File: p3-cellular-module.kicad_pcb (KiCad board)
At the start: 4 copper layers, 40 x 57.4 mm, 57 parts, among them J1 Conn_Coaxial, J2 SIM8060-6-1-14-00-A, J4 Pogo Pins, Q1 BC818, SW1 KMR221GLFS, U1 AP62301WU7, U2 EG25G, U3 USBLC6-2SC6

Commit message: Add: Improved layout
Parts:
- removed J1: Conn_Coaxial, Connector_Coaxial:U.FL_Hirose_U.FL-R-SMT-1_Vertical
- removed R13, R14: DNF, Resistor_SMD:R_0402_1005Metric
- removed TP3: DCD, TestPoint:TestPoint_Pad_D1.5mm
- removed TP4: CTS, TestPoint:TestPoint_Pad_D1.5mm
- removed TP5: RTS, TestPoint:TestPoint_Pad_D1.5mm
- removed TP6: DTR, TestPoint:TestPoint_Pad_D1.5mm
- added E1: NN02-201, NN02-201:XCVR_NN02-201, B.Cu at (130.1, 106.3)
- added REF**: MountingHole_2.2mm_M2_DIN965_Pad, MountingHole:MountingHole_2.2mm_M2_DIN965_Pad, F.Cu at (145.1, 90.9)
- Q1, R5, R6, R7: moved to F.Cu
- TP1, TP10, TP7, TP8, TP9: footprint TestPoint:TestPoint_Pad_D1.5mm -> TestPoint:TestPoint_Pad_1.0x1.0mm
- TP2: value RI -> 3V8; footprint TestPoint:TestPoint_Pad_D1.5mm -> TestPoint:TestPoint_Pad_1.0x1.0mm
- moved TP2 27.2 mm to (133.7, 114.7), turned to 0 degrees
- moved D1 7.38 mm to (135.6, 92.5), turned to 180 degrees
- moved U3 7.37 mm to (140.2, 91.2), turned to -90 degrees
- moved Q1 7.12 mm to (132.0, 90.3), turned to 90 degrees
- moved R7 7.08 mm to (135.5, 90.8)
- moved C18 6.76 mm to (158.8, 109.6), turned to 0 degrees
- moved D2 5.78 mm to (161.8, 106.4)
- moved TP7 5.15 mm to (133.2, 127.0), turned to 90 degrees
- moved R5 3.65 mm to (131.8, 93.2), turned to 0 degrees
- moved R6 3.48 mm to (135.5, 89.1)
- moved R10 3.21 mm to (154.8, 112.1), turned to -90 degrees
- moved TP8 3.01 mm to (133.2, 129.2), turned to 90 degrees
- moved R4 3.00 mm to (161.1, 112.0)
- moved L2 2.30 mm to (128.7, 111.4), turned to -90 degrees
- moved C14 2.06 mm to (131.1, 110.5), turned to 0 degrees
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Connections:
- TP2 pad 1: Net-(TP2-Pad1) -> +3V8
- U2 pad 62: Net-(TP2-Pad1) -> unconnected-(U2-Pad62)
- U2 pad 63: Net-(TP3-Pad1) -> unconnected-(U2-Pad63)
- U2 pad 64: Net-(TP4-Pad1) -> unconnected-(U2-Pad64)
- U2 pad 65: Net-(TP5-Pad1) -> unconnected-(U2-Pad65)
- U2 pad 66: Net-(TP6-Pad1) -> unconnected-(U2-Pad66)
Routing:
- net /Cellular Modem/USIM_RST: track 0.00 -> 43.7 mm, vias 0 -> 1
- net /Cellular Modem/USIM_VDD: track 7.53 -> 46.9 mm, vias 0 -> 7
- net /Cellular Modem/USIM_CLK: track 0.00 -> 32.6 mm, vias 0 -> 1
- net /Cellular Modem/USIM_DATA: track 0.00 -> 29.5 mm, vias 0 -> 1
- net Net-(TP8-Pad1): track 0.00 -> 28.1 mm, vias 0 -> 3
- net Net-(TP7-Pad1): track 0.00 -> 27.8 mm, vias 0 -> 3
- net Net-(C17-Pad1): track 0.00 -> 17.3 mm
- net VBUS: track 15.0 -> 31.5 mm, vias 17 -> 15
- net Net-(C18-Pad1): track 0.45 -> 12.8 mm, vias 0 -> 2
- net +3V8: track 0.00 -> 12.2 mm, vias 10 -> 12
- net Net-(C15-Pad1): track 0.00 -> 11.2 mm, vias 0 -> 2
- net Net-(R2-Pad2): track 0.00 -> 10.1 mm, vias 0 -> 2
- net /USB Connector/USB_DN_RAW: track 6.91 -> 16.0 mm
- net /USB Connector/USB_DP_RAW: track 4.87 -> 12.5 mm
- net Net-(D2-Pad1): track 0.00 -> 7.42 mm, vias 0 -> 2
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- added copper zone on In1.Cu, net VBUS
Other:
- board size 40 x 57.4 mm -> 42 x 57.5 mm
- board text added: "5V"
- board text added: "G"
- board text added: "GND"
- board text added: "LED"
- board text added: "PKY"
- board text added: "U+"
- board text added: "U-"

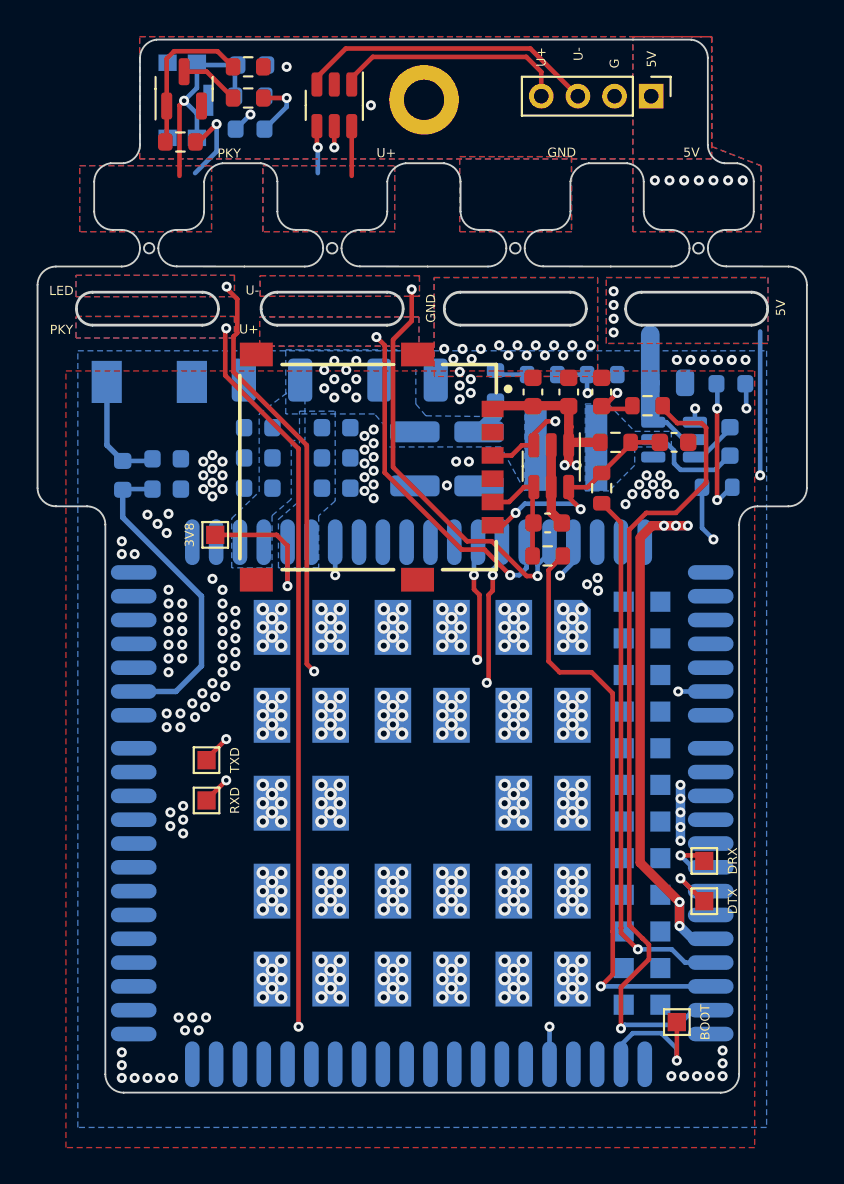
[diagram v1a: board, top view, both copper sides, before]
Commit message: Update: Ground plane setup
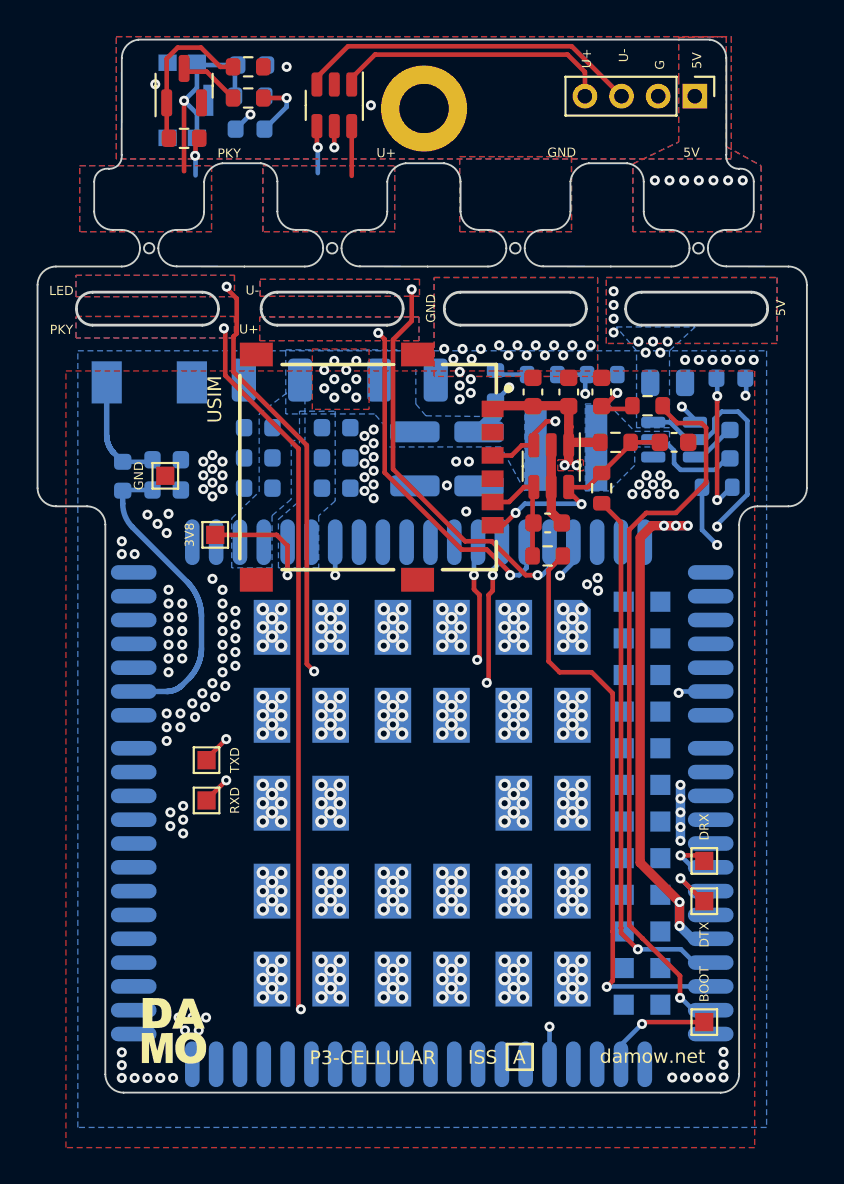
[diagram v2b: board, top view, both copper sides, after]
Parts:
- added G***: LOGO, LOGO, F.Cu at (131.4, 141.7)
- added TP3: GND, TestPoint:TestPoint_Pad_1.0x1.0mm, F.Cu at (131.0, 111.4)
- REF**: value MountingHole_2.2mm_M2_DIN965_Pad -> MountingHole_2.7mm_M2.5_DIN965_Pad; footprint MountingHole:MountingHole_2.2mm_M2_DIN965_Pad -> MountingHole:MountingHole_2.7mm_M2.5_DIN965_Pad
- moved J4 2.38 mm to (159.9, 90.7)
- moved TP1 1.50 mm to (160.4, 141.2)
- moved REF** 0.47 mm to (145.1, 91.4)
- moved D2 0.30 mm to (161.8, 106.1)
- moved R5 0.28 mm to (132.0, 93.0)
- moved Q1 0.17 mm to (132.0, 90.1)
- moved C2 0.15 mm to (161.8, 109.7)
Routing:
- net +3V8: track 12.2 -> 25.6 mm, vias 12 -> 13
- net VBUS: track 31.5 -> 26.2 mm, vias 15 -> 20
- net /Cellular Modem/USIM_RST: track 43.7 -> 38.8 mm
- net /Cellular Modem/NET_STAT_DRV: track 50.0 -> 47.1 mm
- net /USB Connector/USB_DN_RAW: track 16.0 -> 18.5 mm
- net /USB Connector/USB_DP_RAW: track 12.5 -> 15.0 mm
- net Net-(TP7-Pad1): track 27.8 -> 26.2 mm
- net Net-(TP1-Pad1): track 6.42 -> 5.07 mm
- net /Cellular Modem/PWRKEY: track 68.1 -> 67.1 mm
- net /Cellular Modem/USIM_VDD: track 46.9 -> 46.0 mm
- net GND: vias 362 -> 364
- added copper zone on F.Cu, net +3V8
- added copper zone on F.Cu, net /Cellular Modem/USIM_VDD
- added copper zone on In1.Cu, net /Cellular Modem/USIM_VDD
- added copper zone on In1.Cu, net GND
- removed copper zone on In1.Cu, net +3V8
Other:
- outline, holes or cut-outs redrawn
- board text added: "A"
- board text added: "ISS"
- board text added: "P3-CELLULAR"
- board text added: "USIM"
- board text added: "damow.net"

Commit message: Add: Board size changes
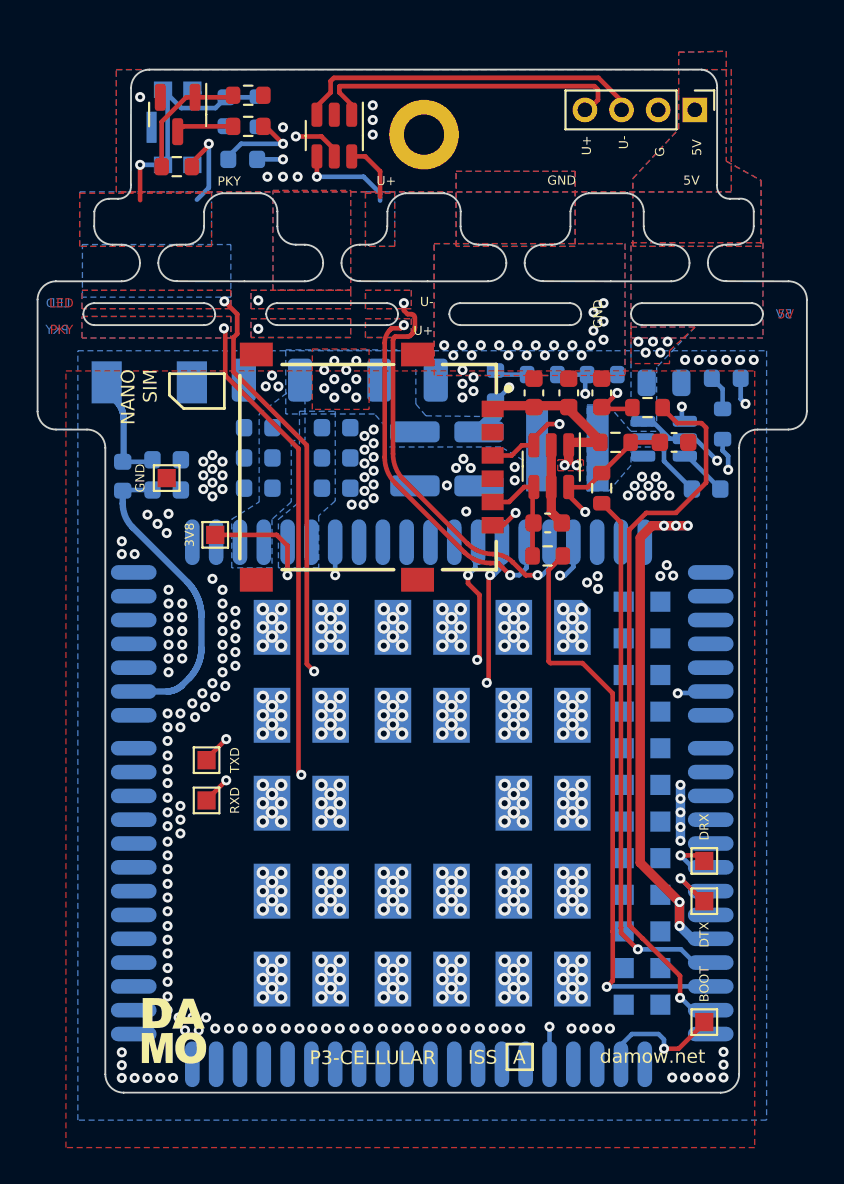
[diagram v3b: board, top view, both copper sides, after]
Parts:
- REF**: value MountingHole_2.7mm_M2.5_DIN965_Pad -> MountingHole_2.2mm_M2_DIN965_Pad; footprint MountingHole:MountingHole_2.7mm_M2.5_DIN965_Pad -> MountingHole:MountingHole_2.2mm_M2_DIN965_Pad
- moved R4 3.46 mm to (161.4, 108.6), turned to -90 degrees
- moved D3 2.91 mm to (134.3, 91.5), turned to 90 degrees
- moved C2 2.77 mm to (160.5, 112.2), turned to 180 degrees
- moved C4 1.96 mm to (153.0, 106.9)
- moved C13 1.90 mm to (151.1, 106.9)
- moved D1 1.70 mm to (135.2, 94.2), turned to 0 degrees
- moved U3 1.65 mm to (140.2, 92.8)
- moved Q1 1.61 mm to (131.7, 91.7), turned to -90 degrees
- moved R5 1.60 mm to (131.6, 94.5)
- moved R6 1.55 mm to (135.5, 90.7)
- moved R7 1.55 mm to (135.5, 92.3)
- moved SW1 1.50 mm to (131.7, 92.4), turned to -90 degrees
- moved REF** 1.42 mm to (145.1, 92.8)
- moved R15 0.96 mm to (136.1, 91.5), turned to -90 degrees
- moved J4 0.75 mm to (159.9, 91.5)
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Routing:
- net Net-(D2-Pad1): track 7.44 -> 1.92 mm, vias 2 -> 0
- net VBUS: track 26.2 -> 22.8 mm, vias 20 -> 9
- net /Cellular Modem/USB_DN: track 24.7 -> 27.4 mm
- net /USB Connector/USB_DP_RAW: track 15.0 -> 17.5 mm
- net /Cellular Modem/NET_STAT_DRV: track 47.1 -> 49.4 mm
- net /Cellular Modem/STAT_OD: track 27.4 -> 29.5 mm
- net /Power Supply/SW: track 5.58 -> 3.58 mm
- net Net-(Q1-Pad1): track 8.78 -> 6.95 mm
- net Net-(D1-Pad1): track 3.48 -> 4.96 mm
- net /Cellular Modem/USB_DP: track 21.7 -> 22.9 mm
- net /Cellular Modem/PWRKEY: track 67.1 -> 68.2 mm
- net Net-(C14-Pad1): track 6.15 -> 5.15 mm
- net Net-(TP1-Pad1): track 5.07 -> 6.05 mm
- net /USB Connector/USB_DN_RAW: track 18.5 -> 19.1 mm
- net /Cellular Modem/USIM_VDD: track 46.0 -> 46.5 mm
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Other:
- board size 42 x 57.5 mm -> 42 x 55.8 mm
- board text added: "NANO SIM"
- board text removed: "USIM"

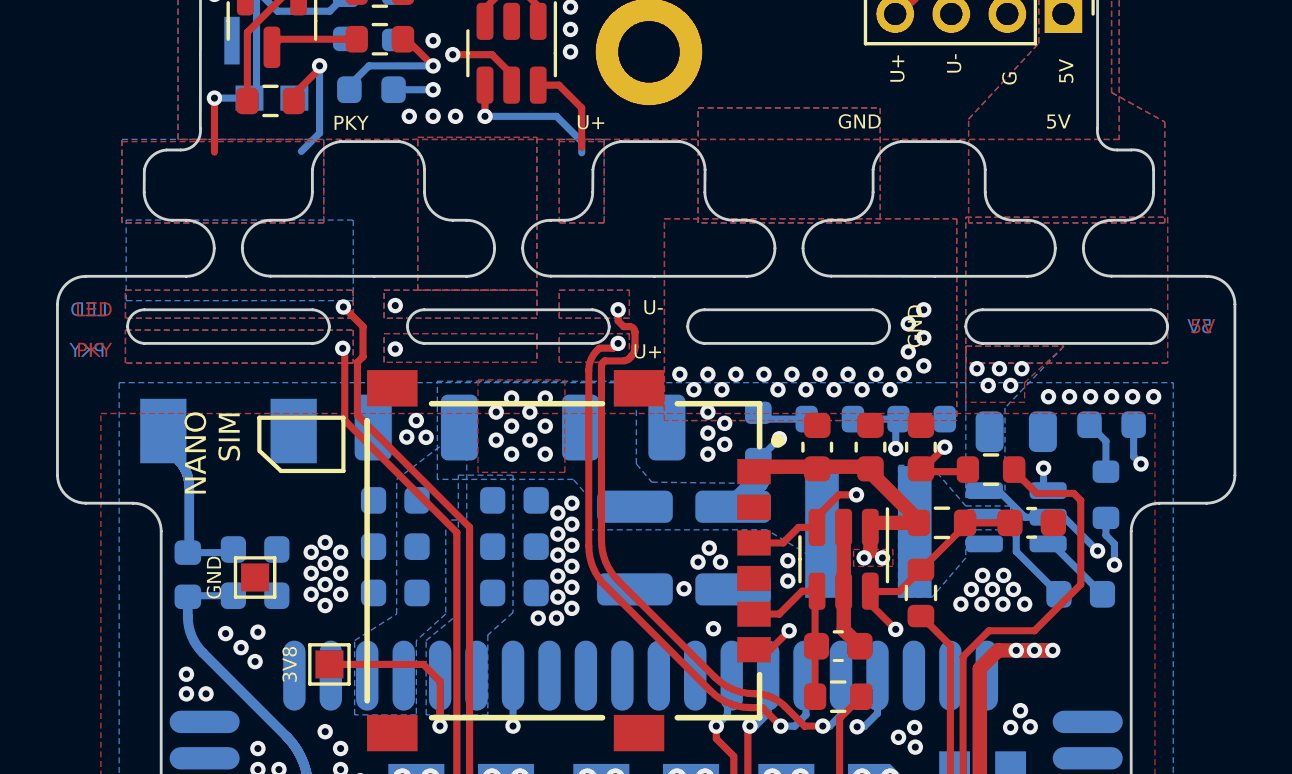
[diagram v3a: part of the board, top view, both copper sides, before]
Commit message: Add: Mechanical changes pre-rev1 production run
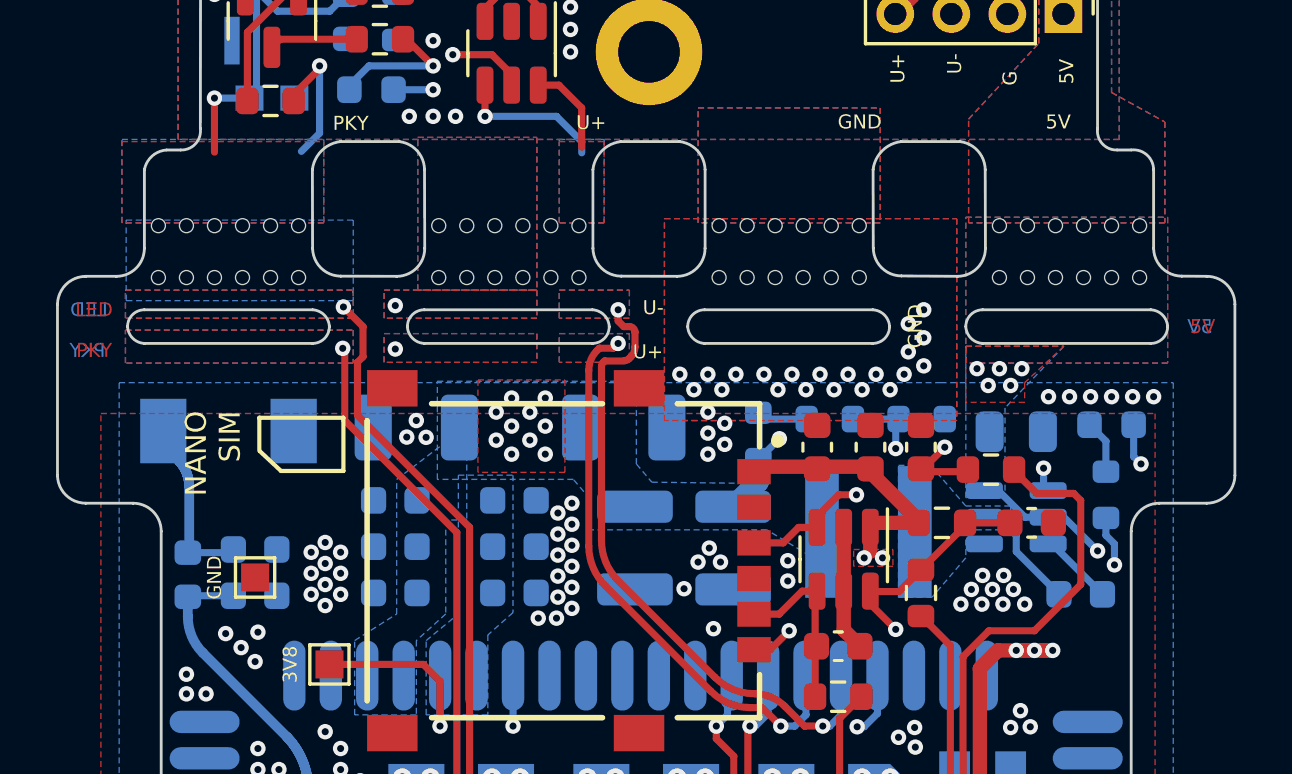
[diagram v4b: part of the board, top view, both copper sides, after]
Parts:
- added REF**: MouseBitHole_0.5mm, p3-cellular-module:MouseBitHole_0.5mm, F.Cu at (141.6, 99.0)
- added REF**: MouseBitHole_0.5mm, p3-cellular-module:MouseBitHole_0.5mm, F.Cu at (147.6, 99.0)
- added REF**: MouseBitHole_0.5mm, p3-cellular-module:MouseBitHole_0.5mm, F.Cu at (128.6, 100.8)
- added REF**: MouseBitHole_0.5mm, p3-cellular-module:MouseBitHole_0.5mm, F.Cu at (132.6, 100.8)
- added REF**: MouseBitHole_0.5mm, p3-cellular-module:MouseBitHole_0.5mm, F.Cu at (159.6, 100.8)
- added REF**: MouseBitHole_0.5mm, p3-cellular-module:MouseBitHole_0.5mm, F.Cu at (127.6, 99.0)
- added REF**: MouseBitHole_0.5mm, p3-cellular-module:MouseBitHole_0.5mm, F.Cu at (132.6, 99.0)
- added REF**: MouseBitHole_0.5mm, p3-cellular-module:MouseBitHole_0.5mm, F.Cu at (141.6, 100.8)
- added REF**: MouseBitHole_0.5mm, p3-cellular-module:MouseBitHole_0.5mm, F.Cu at (162.6, 99.0)
- added REF**: MouseBitHole_0.5mm, p3-cellular-module:MouseBitHole_0.5mm, F.Cu at (142.6, 100.8)
- added REF**: MouseBitHole_0.5mm, p3-cellular-module:MouseBitHole_0.5mm, F.Cu at (149.6, 99.0)
- added REF**: MouseBitHole_0.5mm, p3-cellular-module:MouseBitHole_0.5mm, F.Cu at (148.6, 100.8)
- added REF**: MouseBitHole_0.5mm, p3-cellular-module:MouseBitHole_0.5mm, F.Cu at (139.6, 100.8)
- added REF**: MouseBitHole_0.5mm, p3-cellular-module:MouseBitHole_0.5mm, F.Cu at (152.6, 100.8)
- added REF**: MouseBitHole_0.5mm, p3-cellular-module:MouseBitHole_0.5mm, F.Cu at (131.6, 100.8)
- added REF**: MouseBitHole_0.5mm, p3-cellular-module:MouseBitHole_0.5mm, F.Cu at (161.6, 100.8)
- added REF**: MouseBitHole_0.5mm, p3-cellular-module:MouseBitHole_0.5mm, F.Cu at (158.6, 99.0)
- added REF**: MouseBitHole_0.5mm, p3-cellular-module:MouseBitHole_0.5mm, F.Cu at (151.6, 99.0)
- added REF**: MouseBitHole_0.5mm, p3-cellular-module:MouseBitHole_0.5mm, F.Cu at (140.6, 100.8)
- added REF**: MouseBitHole_0.5mm, p3-cellular-module:MouseBitHole_0.5mm, F.Cu at (148.6, 99.0)
- added REF**: MouseBitHole_0.5mm, p3-cellular-module:MouseBitHole_0.5mm, F.Cu at (128.6, 99.0)
- added REF**: MouseBitHole_0.5mm, p3-cellular-module:MouseBitHole_0.5mm, F.Cu at (140.6, 99.0)
- added REF**: MouseBitHole_0.5mm, p3-cellular-module:MouseBitHole_0.5mm, F.Cu at (161.6, 99.0)
- added REF**: MouseBitHole_0.5mm, p3-cellular-module:MouseBitHole_0.5mm, F.Cu at (138.6, 100.8)
- added REF**: MouseBitHole_0.5mm, p3-cellular-module:MouseBitHole_0.5mm, F.Cu at (131.6, 99.0)
- added REF**: MouseBitHole_0.5mm, p3-cellular-module:MouseBitHole_0.5mm, F.Cu at (130.6, 100.8)
- added REF**: MouseBitHole_0.5mm, p3-cellular-module:MouseBitHole_0.5mm, F.Cu at (160.6, 99.0)
- added REF**: MouseBitHole_0.5mm, p3-cellular-module:MouseBitHole_0.5mm, F.Cu at (129.6, 99.0)
- added REF**: MouseBitHole_0.5mm, p3-cellular-module:MouseBitHole_0.5mm, F.Cu at (147.6, 100.8)
- added REF**: MouseBitHole_0.5mm, p3-cellular-module:MouseBitHole_0.5mm, F.Cu at (157.6, 100.8)
- added REF**: MouseBitHole_0.5mm, p3-cellular-module:MouseBitHole_0.5mm, F.Cu at (138.6, 99.0)
- added REF**: MouseBitHole_0.5mm, p3-cellular-module:MouseBitHole_0.5mm, F.Cu at (162.6, 100.8)
- added REF**: MouseBitHole_0.5mm, p3-cellular-module:MouseBitHole_0.5mm, F.Cu at (157.6, 99.0)
- added REF**: MouseBitHole_0.5mm, p3-cellular-module:MouseBitHole_0.5mm, F.Cu at (139.6, 99.0)
- added REF**: MouseBitHole_0.5mm, p3-cellular-module:MouseBitHole_0.5mm, F.Cu at (149.6, 100.8)
- added REF**: MouseBitHole_0.5mm, p3-cellular-module:MouseBitHole_0.5mm, F.Cu at (151.6, 100.8)
- added REF**: MouseBitHole_0.5mm, p3-cellular-module:MouseBitHole_0.5mm, F.Cu at (159.6, 99.0)
- added REF**: MouseBitHole_0.5mm, p3-cellular-module:MouseBitHole_0.5mm, F.Cu at (127.6, 100.8)
- added REF**: MouseBitHole_0.5mm, p3-cellular-module:MouseBitHole_0.5mm, F.Cu at (137.6, 100.8)
- added REF**: MouseBitHole_0.5mm, p3-cellular-module:MouseBitHole_0.5mm, F.Cu at (150.6, 100.8)
- added REF**: MouseBitHole_0.5mm, p3-cellular-module:MouseBitHole_0.5mm, F.Cu at (150.6, 99.0)
- added REF**: MouseBitHole_0.5mm, p3-cellular-module:MouseBitHole_0.5mm, F.Cu at (130.6, 99.0)
- added REF**: MouseBitHole_0.5mm, p3-cellular-module:MouseBitHole_0.5mm, F.Cu at (137.6, 99.0)
- added REF**: MouseBitHole_0.5mm, p3-cellular-module:MouseBitHole_0.5mm, F.Cu at (158.6, 100.8)
- added REF**: MouseBitHole_0.5mm, p3-cellular-module:MouseBitHole_0.5mm, F.Cu at (129.6, 100.8)
- added REF**: MouseBitHole_0.5mm, p3-cellular-module:MouseBitHole_0.5mm, F.Cu at (152.6, 99.0)
- added REF**: MouseBitHole_0.5mm, p3-cellular-module:MouseBitHole_0.5mm, F.Cu at (160.6, 100.8)
- added REF**: MouseBitHole_0.5mm, p3-cellular-module:MouseBitHole_0.5mm, F.Cu at (142.6, 99.0)
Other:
- outline, holes or cut-outs redrawn
